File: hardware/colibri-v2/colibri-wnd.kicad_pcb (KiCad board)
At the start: 4 copper layers, 120 x 110 mm, 528 parts, among them CN1 XT60-M, CN10 629_105_150_921, CN11 629_105_150_921, CN12 XT60-F, CN2 XT60-F, CN3 AS0B821-S78B-7H, CN4 HDMI_A, CN5 692_121_030_100, CN6 Wurth-68715014522-LCD, CN7 MOLEX_73366_0061, CN8 629_105_150_921, CN9 Wurth-68711814522, CON1 PJ-102AH, P1 CONN_02X10, P10 CONN_01X08, P11 CONN_01X03, P12 CONN_01X03, P13 CONN_01X03, P14 CONN_01X03, P15 CONN_01X03, P16 CONN_01X03, P17 CONN_01X03, P18 CONN_01X03, P19 CONN_01X03, P20 CONN_01X03, P21 CONN_01X03, P22 CONN_01X03, P23 CONN_01X03, P24 CONN_01X03, P25 CONN_01X03, P26 CONN_01X03, P27 CONN_01X03, P28 CONN_01X03, P29 CONN_01X03, P3 CONN_02X01, P30 CONN_01X03, P31 CONN_01X03, P32 CONN_02X10, P33 ECM00870-L, P34 ECM00870-L, P35 STANDOFF, P36 STANDOFF, P37 STANDOFF, P38 STANDOFF, P39 STANDOFF, P4 ECM00870-L, P40 STANDOFF, P5 ECM00870-L, P6 CONN_01X08, P7 CONN_01X04, P8 CONN_01X04, P9 CONN_01X04, Q10 PDTC123JU, Q11 PDTA123JU, Q12 IRLML6402TRPBF, Q13 BSS138PW, Q14 PDTA123JU, Q15 BSS138PW, Q16 BSS138PW, Q17 IRLML6402TRPBF, Q3 BSS138PW, Q4 FDMA530PZ, Q5 BSS138PW, Q6 BSS138PW, Q7 BSS138PW, Q8 AP6681GMT-HF-3TR, Q9 FDMA530PZ, SW1 OMRON B3F-1070, SW10 OMRON B3F-1070, SW11 OMRON B3F-1070, SW2 OMRON B3F-1070, SW3 OMRON B3F-1070, SW4 OMRON B3F-1070, SW5 OMRON B3F-1070, SW6 OMRON B3F-1070, SW7 OMRON B3F-1070, SW8 OMRON B3F-1070, SW9 ALPS-SPPJ320600, U1 L3GD20HTR, U10 TPS2065CDBVT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

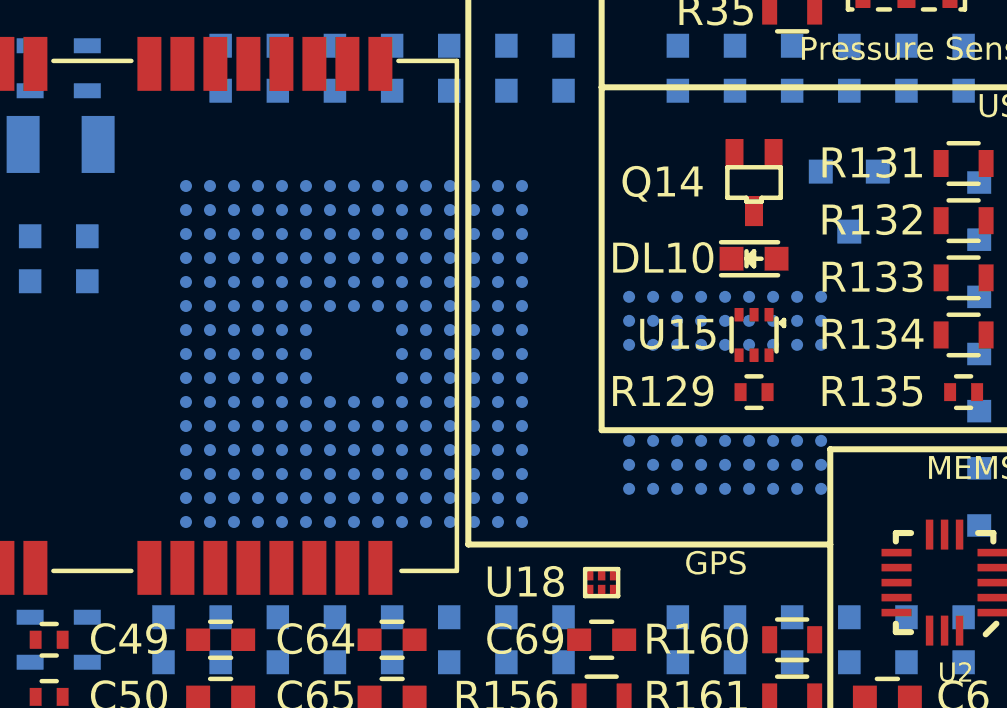
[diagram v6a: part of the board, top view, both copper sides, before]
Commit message: Changed the tfbga footprints to use smaller pads
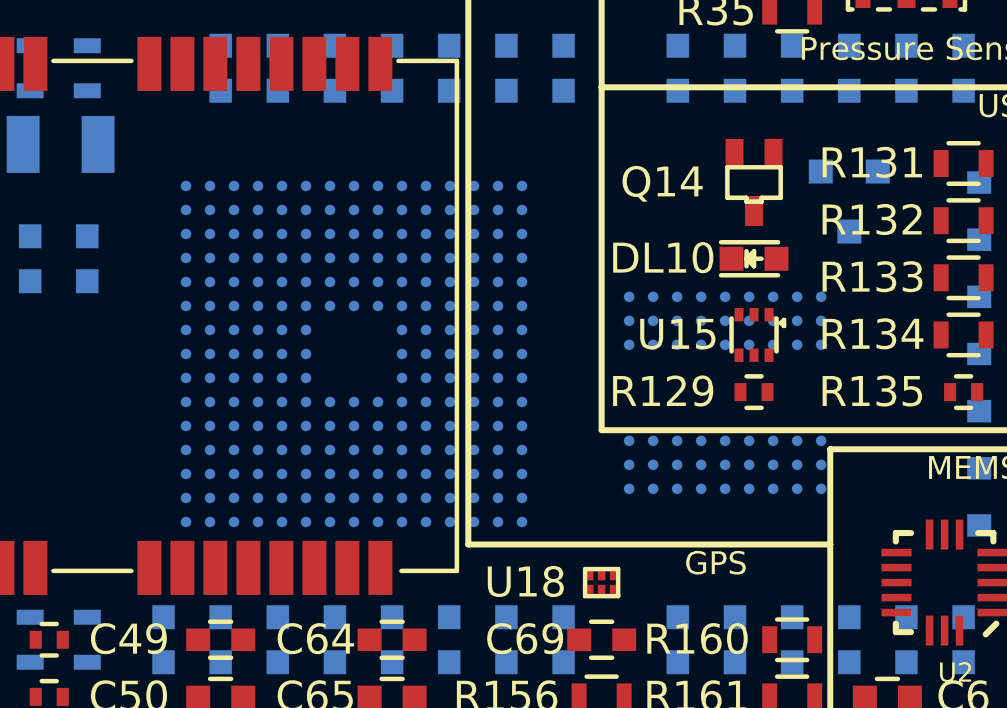
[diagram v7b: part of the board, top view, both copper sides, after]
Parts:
- U25: footprint Sigmadrone:tfbga-216 -> Sigmadrone:tfbga-216-35
- U3: footprint Sigmadrone:tfbga-54 -> Sigmadrone:tfbga-54-35
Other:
- net class Default: clearance 0.12192 -> 0.1905; trace_width 0.254 -> 0.2286; via_dia 0.4826 -> 0.635
- rule trace_clearance: 0.12192 -> 0.1905

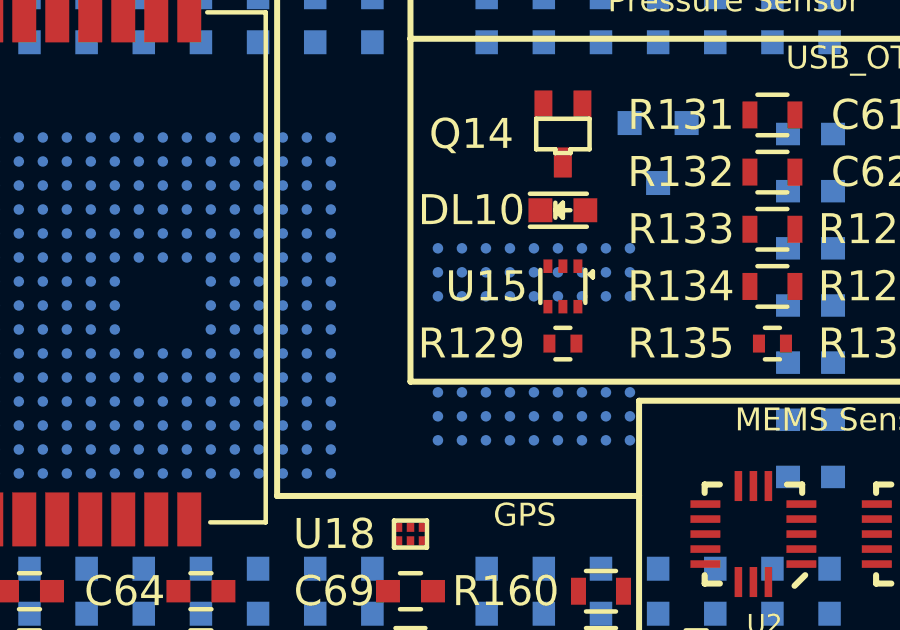
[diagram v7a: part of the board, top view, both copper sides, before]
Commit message: Work on PCB design rules.
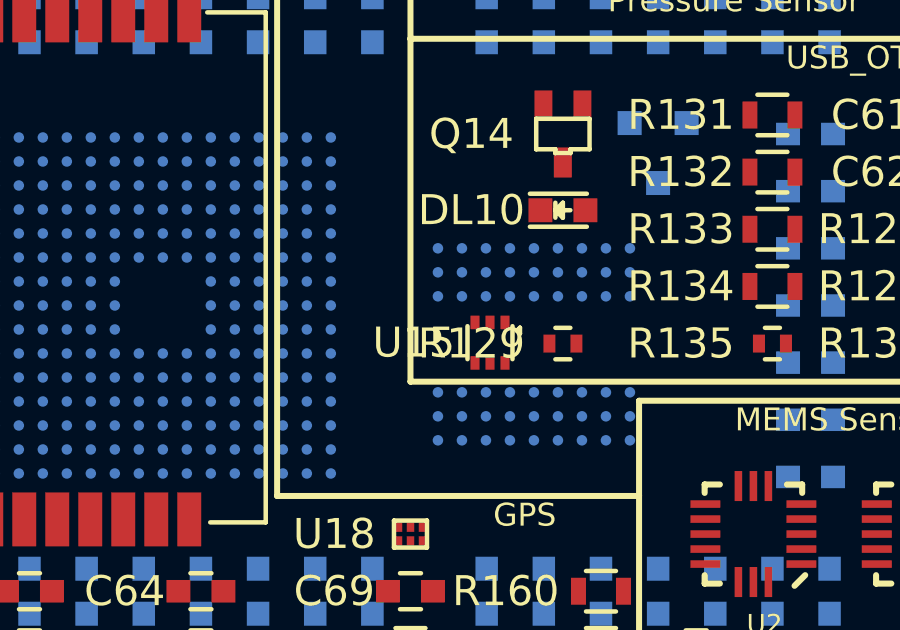
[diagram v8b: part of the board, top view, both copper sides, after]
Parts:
- moved U15 3.07 mm to (90.3, 99.0)
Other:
- net class Default: clearance 0.1905 -> 0.1778; trace_width 0.2286 -> 0.2032; via_dia 0.635 -> 0.889; via_drill 0.3429 -> 0.635
- net class Power: clearance 0.3 -> 0.2032; trace_width 0.8 -> 0.254; via_dia 1.3 -> 0.889; via_drill 0.8 -> 0.635
- rule trace_clearance: 0.1905 -> 0.1778
- rule trace_min: 0.12 -> 0.1524
- rule via_min_drill: 0.25 -> 0.3302
- rule via_min_size: 0.4 -> 0.508
